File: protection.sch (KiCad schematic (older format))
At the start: 11 parts, among them Q1 WST03P06, U7 H7550-H#

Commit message: Update components according to JLCPCB availability
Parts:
- D1: value 5.0SMDJ36CA -> 5.0SMDJ33CA; LCSC C284112 -> C112941
- D10: value SMBJ36CA -> SMBJ33CA; LCSC C114002 -> C143164
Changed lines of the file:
@@
 P 3000 1600
 F 0 "D1" V 2954 1679 50  0000 L CNN
-F 1 "5.0SMDJ36CA" V 3045 1679 50  0000 L CNN
+F 1 "5.0SMDJ33CA" V 3045 1679 50  0000 L CNN
 F 2 "Diode_SMD:D_SMC" H 3000 1600 50  0001 C CNN
 F 3 "~" H 3000 1600 50  0001 C CNN
-F 4 "C284112" H 3000 1600 50  0001 C CNN "LCSC"
+F 4 "C112941" H 3000 1600 50  0001 C CNN "LCSC"
 	1    3000 1600
 	0    1    1    0
@@
 AR Path="/5E460E30/5F59D8F4" Ref="D10"  Part="1"
 F 0 "D10" V 2354 4529 50  0000 L CNN
-F 1 "SMBJ36CA" V 2445 4529 50  0000 L CNN
+F 1 "SMBJ33CA" V 2445 4529 50  0000 L CNN
 F 2 "Diode_SMD:D_SMB" H 2400 4450 50  0001 C CNN
 F 3 "~" H 2400 4450 50  0001 C CNN
-F 4 "C114002" H 2400 4450 50  0001 C CNN "LCSC"
+F 4 "C143164" H 2400 4450 50  0001 C CNN "LCSC"
 	1    2400 4450
 	0    1    1    0

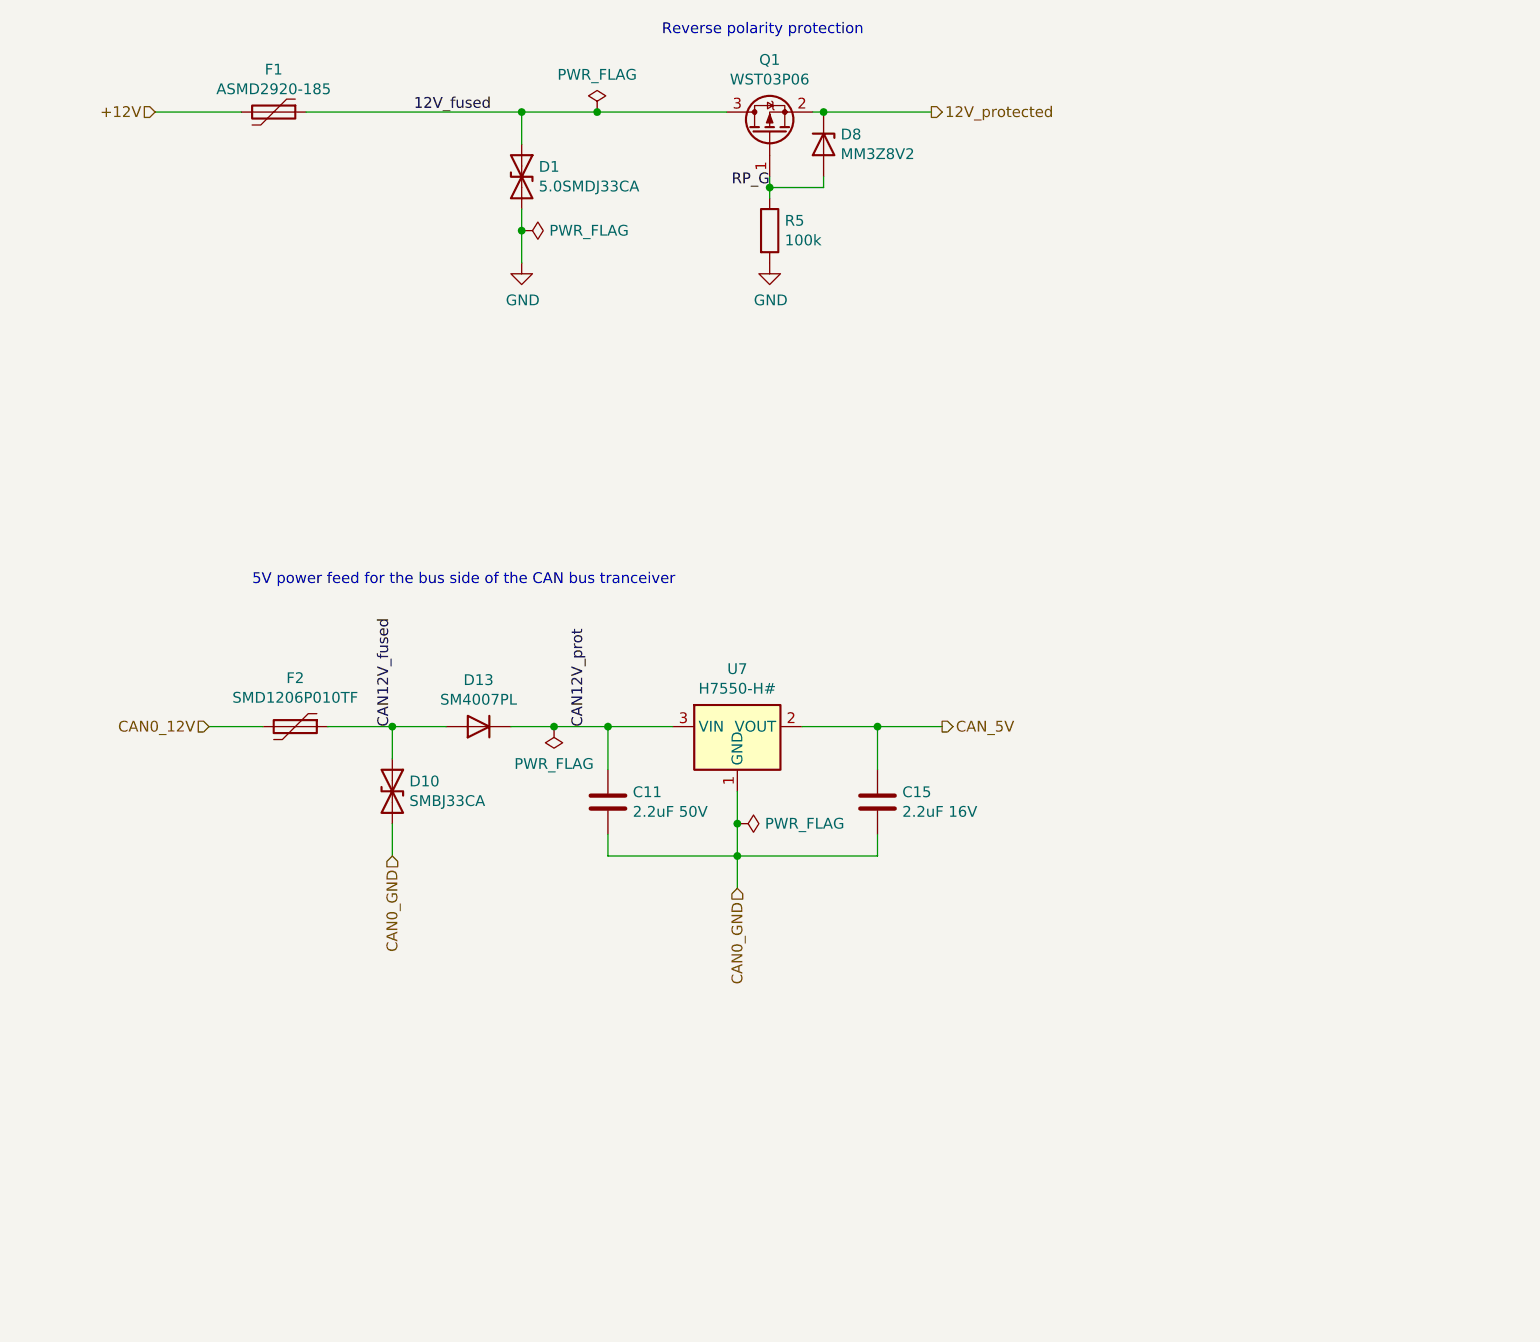
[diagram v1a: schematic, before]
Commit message: Schema updated
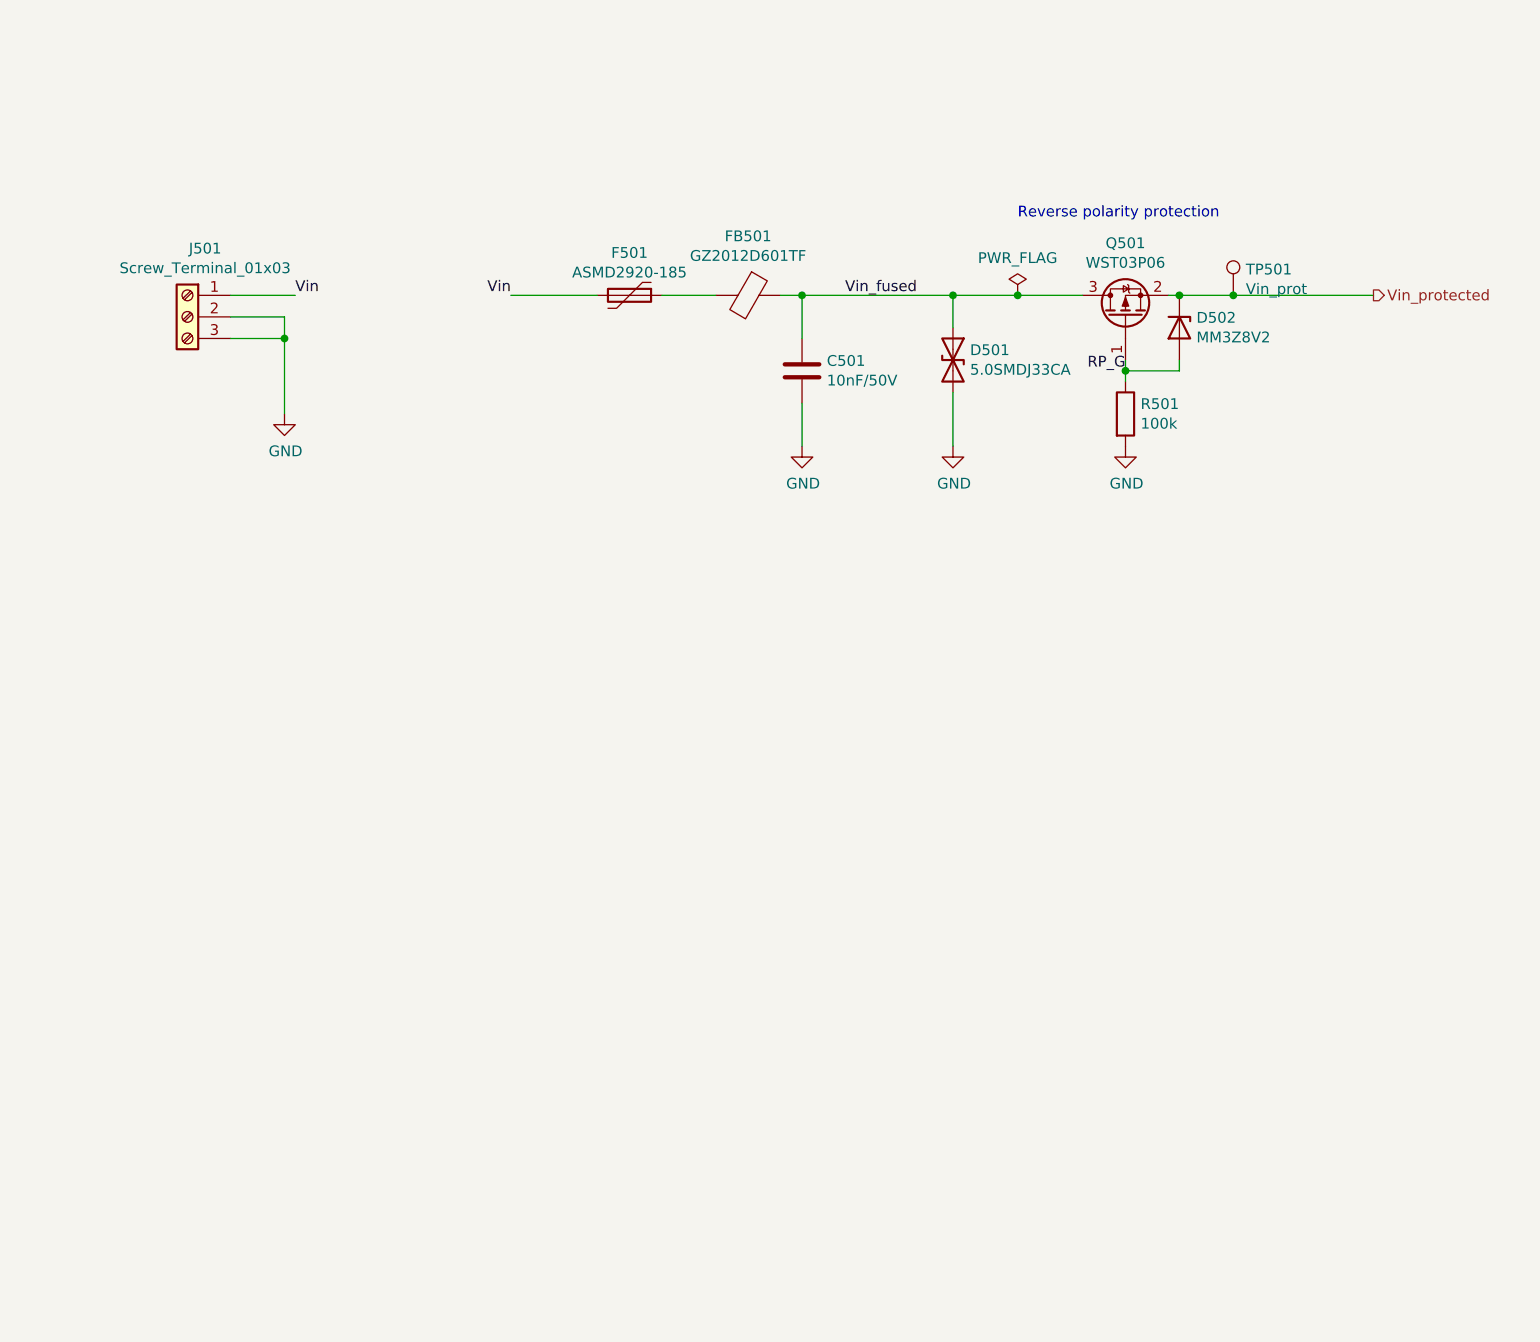
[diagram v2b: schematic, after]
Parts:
- removed C11: 2.2uF 50V, Capacitor_SMD:C_1206_3216Metric, symbol Device:C
- removed C15: 2.2uF 16V, Capacitor_SMD:C_0603_1608Metric, symbol Device:C
- removed D10: SMBJ33CA, Diode_SMD:D_SMB, symbol Device:D_TVS
- removed D13: SM4007PL, Diode_SMD:D_SOD-123F, symbol Device:D
- removed F2: SMD1206P010TF, Fuse:Fuse_1206_3216Metric, symbol Device:Polyfuse
- removed U7: H7550-H#, Package_TO_SOT_SMD:SOT-23, symbol sailor-hat:HT75xx-1-SOT23
- added C501: 10nF/50V, Capacitor_SMD:C_0402_1005Metric, symbol Device:C
- added FB501: GZ2012D601TF, Inductor_SMD:L_0805_2012Metric, symbol Device:Ferrite_Bead
- added J501: Screw_Terminal_01x03, symbol Connector:Screw_Terminal_01x03
- added TP501: Vin_prot, TestPoint:TestPoint_Keystone_5000-5004_Miniature, symbol Connector:TestPoint
- renumbered D1 to D501, D8 to D502, F1 to F501, Q1 to Q501, R5 to R501
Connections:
- net GND: now also C501.2, J501.2 (Pin_2), J501.3 (Pin_3)
- net +12V renamed Vin
- net Vin: now also J501.1 (Pin_1)
- net 12V_fused renamed Vin_fused
- net Vin_fused: now also C501.1, FB501.1; no longer F501.1
- net 12V_protected renamed Vin_protected
- net Vin_protected: now also TP501.1
- new net: F501.1, FB501.2
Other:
- note removed: "5V power feed for the bus side of the CAN bus tranceiver"
- moved on the sheet: D501, D502, F501, Q501, R501

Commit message: Redesigned layout to take EMC issues better into account
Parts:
- J501: footprint (none) -> Connector_Phoenix_MC:PhoenixContact_MC_1,5_3-G-3.81_1x03_P3.81mm_Horizontal
- R501: footprint Resistor_SMD:R_0603_1608Metric -> Resistor_SMD:R_0402_1005Metric; LCSC C25803 -> C25741
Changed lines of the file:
@@
 $Descr A4 11693 8268
 encoding utf-8
-Sheet 5 8
+Sheet 5 9
 Title "Sailor Hat for Raspberry Pi"
 Date ""
@@
 F 0 "R501" H 5870 2746 50  0000 L CNN
 F 1 "100k" H 5870 2655 50  0000 L CNN
-F 2 "Resistor_SMD:R_0603_1608Metric" V 5730 2700 50  0001 C CNN
+F 2 "Resistor_SMD:R_0402_1005Metric" V 5730 2700 50  0001 C CNN
 F 3 "~" H 5800 2700 50  0001 C CNN
-F 4 "C25803" H 5800 2700 50  0001 C CNN "LCSC"
+F 4 "C25741" H 5800 2700 50  0001 C CNN "LCSC"
 	1    5800 2700
 	1    0    0    -1
@@
 F 0 "J501" H 1368 2567 50  0000 C CNN
 F 1 "Screw_Terminal_01x03" H 1368 2476 50  0000 C CNN
-F 2 "" H 1450 2250 50  0001 C CNN
+F 2 "Connector_Phoenix_MC:PhoenixContact_MC_1,5_3-G-3.81_1x03_P3.81mm_Horizontal" H 1450 2250 50  0001 C CNN
 F 3 "~" H 1450 2250 50  0001 C CNN
 	1    1450 2250

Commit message: Make power connector identical to SH-ESP32 for consistency
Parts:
- J501: value Screw_Terminal_01x03 -> Screw_Terminal_01x02; footprint Connector_Phoenix_MC:PhoenixContact_MC_1,5_3-G-3.81_1x03_P3.81mm_Horizontal -> Connector_Phoenix_MC:PhoenixContact_MC_1,5_2-G-3.81_1x02_P3.81mm_Horizontal; symbol Connector:Screw_Terminal_01x03 -> Connector:Screw_Terminal_01x02
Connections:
- net GND: no longer J501.3 (Pin_3)
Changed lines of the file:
@@
 	4300 2150 5000 2150
 $Comp
-L Connector:Screw_Terminal_01x03 J501
+L Connector:Screw_Terminal_01x02 J501
 U 1 1 5FB8FE7E
-P 1450 2250
-F 0 "J501" H 1368 2567 50  0000 C CNN
-F 1 "Screw_Terminal_01x03" H 1368 2476 50  0000 C CNN
-F 2 "Connector_Phoenix_MC:PhoenixContact_MC_1,5_3-G-3.81_1x03_P3.81mm_Horizontal" H 1450 2250 50  0001 C CNN
-F 3 "~" H 1450 2250 50  0001 C CNN
-	1    1450 2250
+P 1450 2150
+F 0 "J501" H 1368 2467 50  0000 C CNN
+F 1 "Screw_Terminal_01x02" H 1368 2376 50  0000 C CNN
+F 2 "Connector_Phoenix_MC:PhoenixContact_MC_1,5_2-G-3.81_1x02_P3.81mm_Horizontal" H 1450 2150 50  0001 C CNN
+F 3 "~" H 1450 2150 50  0001 C CNN
+	1    1450 2150
 	-1   0    0    -1
 $EndComp
@@
 $EndComp
 Wire Wire Line
-	1900 2700 1900 2350
-Wire Wire Line
-	1900 2350 1650 2350
-Wire Wire Line
 	1650 2250 1900 2250
 Wire Wire Line
-	1900 2250 1900 2350
-Connection ~ 1900 2350
+	1950 2150 1650 2150
 Wire Wire Line
-	1950 2150 1650 2150
+	1900 2250 1900 2700
 $EndSCHEMATC

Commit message: Add missing LCSC part numbers
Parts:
- J501: LCSC (none) -> C8387
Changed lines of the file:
@@
 F 2 "Connector_Phoenix_MC:PhoenixContact_MC_1,5_2-G-3.81_1x02_P3.81mm_Horizontal" H 1450 2150 50  0001 C CNN
 F 3 "~" H 1450 2150 50  0001 C CNN
+F 4 "C8387" H 1450 2150 50  0001 C CNN "LCSC"
 	1    1450 2150
 	-1   0    0    -1

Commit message: Extend the PCB size to provide space for an onboard supercapacitor
The PCB was extended to the left by 21mm to provide room for a
18x40mm (max 18x42mm) 50/60F supercapacitor. The supercapacitor
is lodged in a slot on the PCB to provide mechanical stability and limit
the maximum height of the assembly. It now requires 14mm of headroom.

Additionally, the following changes were made:

- the external supercap connector was removed
- the power and CAN connectors were swapped to JST XH
- there is space for a wire link between CAN and power conx
- power protection circuitry was moved to the edge of the board
- 3.3V regulator was moved to improve the layout
- a 100pF cap was added to the boost feedback to improve loop stability
- rectangles were drawn around ground pins on the GPIO connector
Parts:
- added J502: Wire Link, SH-RPi:WireLink_1x02_P2.54mm, symbol Connector_Generic:Conn_01x02
- J501: value Screw_Terminal_01x02 -> JST XH horiz; footprint Connector_Phoenix_MC:PhoenixContact_MC_1,5_2-G-3.81_1x02_P3.81mm_Horizontal -> SH-RPi:Boomelec_XH-2AW_1x02_P2.50mm_Horiz; symbol Connector:Screw_Terminal_01x02 -> Connector_Generic:Conn_01x02; LCSC C8387 -> C33132
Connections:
- wire segments 20 -> 23
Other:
- note added: "Optional wire link to power the\nboard from NMEA 2000"
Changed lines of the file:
@@
 Title "Sailor Hat for Raspberry Pi"
 Date ""
-Rev "revL"
+Rev "revM"
 Comp "Hat Laboratories"
 Comment1 "https://creativecommons.org/licenses/by-sa/4.0"
@@
 	4300 2150 5000 2150
 $Comp
-L Connector:Screw_Terminal_01x02 J501
+L Connector_Generic:Conn_01x02 J501
 U 1 1 5FB8FE7E
-P 1450 2150
-F 0 "J501" H 1368 2467 50  0000 C CNN
-F 1 "Screw_Terminal_01x02" H 1368 2376 50  0000 C CNN
-F 2 "Connector_Phoenix_MC:PhoenixContact_MC_1,5_2-G-3.81_1x02_P3.81mm_Horizontal" H 1450 2150 50  0001 C CNN
-F 3 "~" H 1450 2150 50  0001 C CNN
-F 4 "C8387" H 1450 2150 50  0001 C CNN "LCSC"
-	1    1450 2150
-	-1   0    0    -1
+P 1450 2250
+F 0 "J501" H 1368 2567 50  0000 C CNN
+F 1 "JST XH horiz" H 1368 2476 50  0000 C CNN
+F 2 "SH-RPi:Boomelec_XH-2AW_1x02_P2.50mm_Horiz" H 1450 2250 50  0001 C CNN
+F 3 "~" H 1450 2250 50  0001 C CNN
+F 4 "C33132" H 1450 2250 50  0001 C CNN "LCSC"
+	1    1450 2250
+	-1   0    0    1
 $EndComp
 Text Label 2950 2150 2    50   ~ 0
@@
 Wire Wire Line
 	1900 2250 1900 2700
+$Comp
+L Connector_Generic:Conn_01x02 J502
+U 1 1 5FCFA451
+P 1500 3450
+F 0 "J502" H 1418 3125 50  0000 C CNN
+F 1 "Wire Link" H 1418 3216 50  0000 C CNN
+F 2 "SH-RPi:WireLink_1x02_P2.54mm" H 1418 3217 50  0001 C CNN
+F 3 "~" H 1500 3450 50  0001 C CNN
+	1    1500 3450
+	-1   0    0    1
+$EndComp
+Text Label 2000 3350 0    50   ~ 0
+Vin
+$Comp
+L power:GND #PWR?
+U 1 1 5FCFC5D6
+P 1950 3900
+AR Path="/5FCFC5D6" Ref="#PWR?"  Part="1"
+AR Path="/5C3476D8/5FCFC5D6" Ref="#PWR?"  Part="1"
+AR Path="/5E460E30/5FCFC5D6" Ref="#PWR0505"  Part="1"
+F 0 "#PWR0505" H 1950 3650 50  0001 C CNN
+F 1 "GND" H 1955 3727 50  0000 C CNN
+F 2 "" H 1950 3900 50  0001 C CNN
+F 3 "" H 1950 3900 50  0001 C CNN
+	1    1950 3900
+	1    0    0    -1
+$EndComp
+Wire Wire Line
+	1700 3450 1950 3450
+Wire Wire Line
+	2000 3350 1700 3350
+Wire Wire Line
+	1950 3450 1950 3900
+Text Notes 2400 3600 0    50   ~ 0
+Optional wire link to power the\nboard from NMEA 2000
 $EndSCHEMATC

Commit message: Replace polyfuse with a regular fuse
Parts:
- removed F501: ASMD2920-185, Fuse:Fuse_2920_7451Metric, symbol Device:Polyfuse
- added F501: 12H1200C, Fuse:Fuse_1206_3216Metric, symbol Device:Fuse
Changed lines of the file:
@@
 Comment4 ""
 $EndDescr
-$Comp
-L Device:Polyfuse F?
-U 1 1 5E467AC2
-P 3500 2150
-AR Path="/5E467AC2" Ref="F?"  Part="1"
-AR Path="/5C3476D8/5E467AC2" Ref="F?"  Part="1"
-AR Path="/5E460E30/5E467AC2" Ref="F501"  Part="1"
-F 0 "F501" V 3303 2150 50  0000 C CNN
-F 1 "ASMD2920-185" V 3394 2150 50  0000 C CNN
-F 2 "Fuse:Fuse_2920_7451Metric" V 3430 2150 50  0001 C CNN
-F 3 "~" H 3500 2150 50  0001 C CNN
-F 4 "C135379" H 3500 2150 50  0001 C CNN "LCSC"
-	1    3500 2150
-	0    1    1    0
-$EndComp
 Text Label 4500 2150 0    50   ~ 0
 Vin_fused
@@
 Text Notes 2400 3600 0    50   ~ 0
 Optional wire link to power the\nboard from NMEA 2000
+$Comp
+L Device:Fuse F501
+U 1 1 601404CD
+P 3500 2150
+F 0 "F501" V 3303 2150 50  0000 C CNN
+F 1 "12H1200C" V 3394 2150 50  0000 C CNN
+F 2 "Fuse:Fuse_1206_3216Metric" V 3430 2150 50  0001 C CNN
+F 3 "~" H 3500 2150 50  0001 C CNN
+F 4 "C182310" V 3500 2150 50  0001 C CNN "LCSC"
+	1    3500 2150
+	0    1    1    0
+$EndComp
 $EndSCHEMATC

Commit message: IN PROGRESS
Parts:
- added C?: 10nF/50V, symbol Device:C
- C501: footprint Capacitor_SMD:C_0402_1005Metric -> (none); LCSC C15195 -> (none)
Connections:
- wire segments 23 -> 26
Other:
- moved on the sheet: C501, D501, D502, F501, FB501, Q501, R501, TP501
